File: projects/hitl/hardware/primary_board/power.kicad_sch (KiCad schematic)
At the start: 11 parts

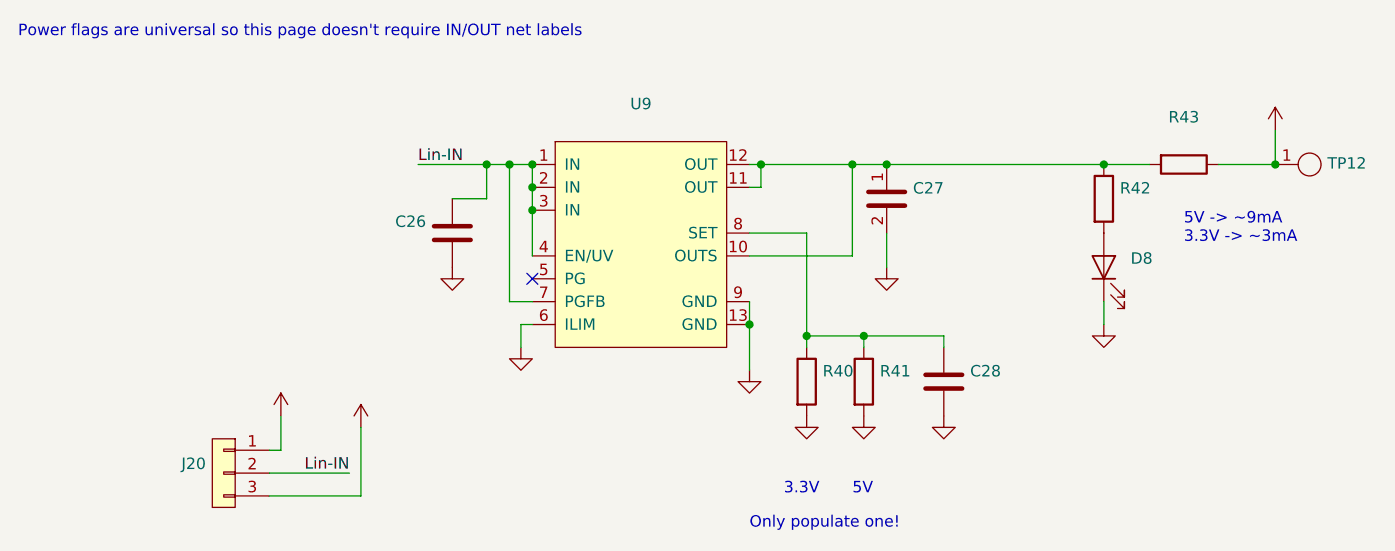
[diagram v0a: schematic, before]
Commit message: chore: annotate migrated schematics
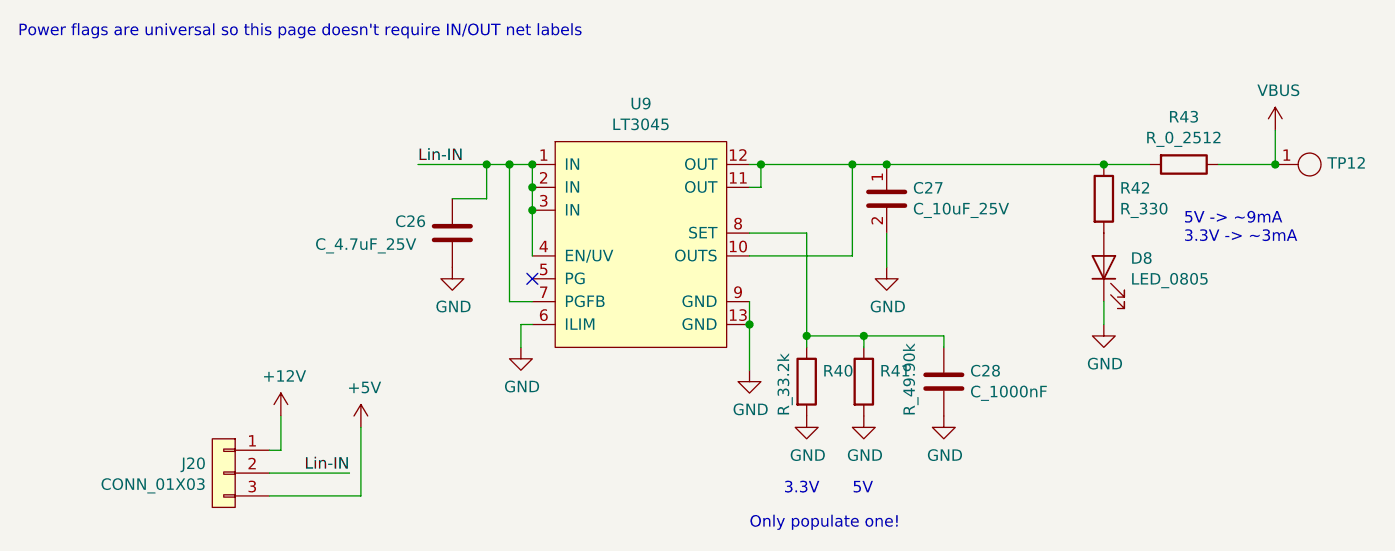
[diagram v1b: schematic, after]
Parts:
- C26: value (none) -> C_4.7uF_25V; footprint (none) -> footprints:C_0805_OEM
- C27: value (none) -> C_10uF_25V; footprint (none) -> footprints:C_0805_OEM
- C28: value (none) -> C_1000nF; footprint (none) -> footprints:C_0603_1608Metric
- D8: value (none) -> LED_0805; footprint (none) -> footprints:LED_0805_OEM
- J20: value (none) -> CONN_01X03; footprint (none) -> footprints:PinHeader_1x03_P2.54mm_Vertical
- R40: value (none) -> R_33.2k; footprint (none) -> footprints:R_0805_OEM
- R41: value (none) -> R_49.90k; footprint (none) -> footprints:R_0805_OEM
- R42: value (none) -> R_330; footprint (none) -> footprints:R_0805_OEM
- R43: value (none) -> R_0_2512; footprint (none) -> footprints:R_2512_OEM
- TP12: value (none) -> Test_Point_SMD; footprint (none) -> footprints:Test_Point_SMD
- U9: value (none) -> LT3045; footprint (none) -> footprints:MSOP-12_MSE
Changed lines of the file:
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@@
     (in_bom yes) (on_board yes)
     (property "Reference" "U9" (id 0) (at 140.335 59.309 0))
-    (property "Value" "" (id 1) (at 140.335 61.6204 0))
-    (property "Footprint" "" (id 2) (at 121.92 17.78 0)
+    (property "Value" "LT3045" (id 1) (at 140.335 61.6204 0))
+    (property "Footprint" "footprints:MSOP-12_MSE" (id 2) (at 121.92 17.78 0)
       (effects (font (size 1.27 1.27) italic) hide)
     )
@@
       (effects (font (size 1.27 1.27)) hide)
     )
-    (property "Value" "" (id 1) (at 109.601 90.8558 0))
+    (property "Value" "+5V" (id 1) (at 109.601 90.8558 0))
     (property "Footprint" "" (id 2) (at 109.22 95.25 0)
       (effects (font (size 1.27 1.27)) hide)
@@
       (effects (font (size 1.27 1.27)) hide)
     )
-    (property "Value" "" (id 1) (at 211.201 57.8358 0))
+    (property "Value" "VBUS" (id 1) (at 211.201 57.8358 0))
     (property "Footprint" "" (id 2) (at 210.82 62.23 0)
       (effects (font (size 1.27 1.27)) hide)
@@
       (effects (font (size 1.27 1.27)) (justify left))
     )
-    (property "Value" "" (id 1) (at 104.14 74.93 0)
-      (effects (font (size 1.27 1.27)) (justify left))
-    )
-    (property "Footprint" "" (id 2) (at 120.3452 59.69 0)
+    (property "Value" "C_4.7uF_25V" (id 1) (at 104.14 74.93 0)
+      (effects (font (size 1.27 1.27)) (justify left))
+    )
+    (property "Footprint" "footprints:C_0805_OEM" (id 2) (at 120.3452 59.69 0)
       (effects (font (size 1.27 1.27)) hide)
     )
@@
       (effects (font (size 1.27 1.27)) hide)
     )
-    (property "Value" "" (id 1) (at 119.507 81.8642 0))
+    (property "Value" "GND" (id 1) (at 119.507 81.8642 0))
     (property "Footprint" "" (id 2) (at 119.38 77.47 0)
       (effects (font (size 1.27 1.27)) hide)
@@
       (effects (font (size 1.27 1.27)) hide)
     )
-    (property "Value" "" (id 1) (at 127.127 90.7542 0))
+    (property "Value" "GND" (id 1) (at 127.127 90.7542 0))
     (property "Footprint" "" (id 2) (at 127 86.36 0)
       (effects (font (size 1.27 1.27)) hide)
@@
       (effects (font (size 1.27 1.27)) (justify left))
     )
-    (property "Value" "" (id 1) (at 170.561 70.993 0)
-      (effects (font (size 1.27 1.27)) (justify left))
-    )
-    (property "Footprint" "" (id 2) (at 166.37 74.93 0)
+    (property "Value" "C_10uF_25V" (id 1) (at 170.561 70.993 0)
+      (effects (font (size 1.27 1.27)) (justify left))
+    )
+    (property "Footprint" "footprints:C_0805_OEM" (id 2) (at 166.37 74.93 0)
       (effects (font (size 1.27 1.27)) hide)
     )
@@
       (effects (font (size 1.27 1.27)) hide)
     )
-    (property "Value" "" (id 1) (at 152.527 93.2942 0))
+    (property "Value" "GND" (id 1) (at 152.527 93.2942 0))
     (property "Footprint" "" (id 2) (at 152.4 88.9 0)
       (effects (font (size 1.27 1.27)) hide)
@@
       (effects (font (size 1.27 1.27)) hide)
     )
-    (property "Value" "" (id 1) (at 100.711 89.5858 0))
+    (property "Value" "+12V" (id 1) (at 100.711 89.5858 0))
     (property "Footprint" "" (id 2) (at 100.33 93.98 0)
       (effects (font (size 1.27 1.27)) hide)
@@
       (effects (font (size 1.27 1.27)) (justify left))
     )
-    (property "Value" "" (id 1) (at 91.9988 101.6 0)
-      (effects (font (size 1.27 1.27)) (justify left))
-    )
-    (property "Footprint" "" (id 2) (at 92.71 130.81 0)
+    (property "Value" "CONN_01X03" (id 1) (at 91.9988 101.6 0)
+      (effects (font (size 1.27 1.27)) (justify left))
+    )
+    (property "Footprint" "footprints:PinHeader_1x03_P2.54mm_Vertical" (id 2) (at 92.71 130.81 0)
       (effects (font (size 1.27 1.27)) hide)
     )
@@
       (effects (font (size 1.27 1.27)) (justify left))
     )
-    (property "Value" "" (id 1) (at 170.18 93.98 90)
-      (effects (font (size 1.27 1.27)) (justify left))
-    )
-    (property "Footprint" "" (id 2) (at 163.322 77.47 0)
+    (property "Value" "R_49.90k" (id 1) (at 170.18 93.98 90)
+      (effects (font (size 1.27 1.27)) (justify left))
+    )
+    (property "Footprint" "footprints:R_0805_OEM" (id 2) (at 163.322 77.47 0)
       (effects (font (size 1.27 1.27)) hide)
     )
@@
       (effects (font (size 1.27 1.27)) (justify left))
     )
-    (property "Value" "" (id 1) (at 156.21 93.98 90)
-      (effects (font (size 1.27 1.27)) (justify left))
-    )
-    (property "Footprint" "" (id 2) (at 156.972 77.47 0)
+    (property "Value" "R_33.2k" (id 1) (at 156.21 93.98 90)
+      (effects (font (size 1.27 1.27)) (justify left))
+    )
+    (property "Footprint" "footprints:R_0805_OEM" (id 2) (at 156.972 77.47 0)
       (effects (font (size 1.27 1.27)) hide)
     )
@@
       (effects (font (size 1.27 1.27)) hide)
     )
-    (property "Value" "" (id 1) (at 165.227 98.3742 0))
+    (property "Value" "GND" (id 1) (at 165.227 98.3742 0))
     (property "Footprint" "" (id 2) (at 165.1 93.98 0)
       (effects (font (size 1.27 1.27)) hide)
@@
       (effects (font (size 1.27 1.27)) hide)
     )
-    (property "Value" "" (id 1) (at 158.877 98.3742 0))
+    (property "Value" "GND" (id 1) (at 158.877 98.3742 0))
     (property "Footprint" "" (id 2) (at 158.75 93.98 0)
       (effects (font (size 1.27 1.27)) hide)
@@
       (effects (font (size 1.27 1.27)) (justify left))
     )
-    (property "Value" "" (id 1) (at 176.911 91.313 0)
-      (effects (font (size 1.27 1.27)) (justify left))
-    )
-    (property "Footprint" "" (id 2) (at 174.9552 93.98 0)
+    (property "Value" "C_1000nF" (id 1) (at 176.911 91.313 0)
+      (effects (font (size 1.27 1.27)) (justify left))
+    )
+    (property "Footprint" "footprints:C_0603_1608Metric" (id 2) (at 174.9552 93.98 0)
       (effects (font (size 1.27 1.27)) hide)
     )
@@
       (effects (font (size 1.27 1.27)) hide)
     )
-    (property "Value" "" (id 1) (at 167.767 81.8642 0))
+    (property "Value" "GND" (id 1) (at 167.767 81.8642 0))
     (property "Footprint" "" (id 2) (at 167.64 77.47 0)
       (effects (font (size 1.27 1.27)) hide)
@@
       (effects (font (size 1.27 1.27)) hide)
     )
-    (property "Value" "" (id 1) (at 174.117 98.3742 0))
+    (property "Value" "GND" (id 1) (at 174.117 98.3742 0))
     (property "Footprint" "" (id 2) (at 173.99 93.98 0)
       (effects (font (size 1.27 1.27)) hide)
@@
     (in_bom yes) (on_board yes)
     (property "Reference" "R43" (id 0) (at 200.66 60.7822 90))
-    (property "Value" "" (id 1) (at 200.66 63.0936 90))
-    (property "Footprint" "" (id 2) (at 200.66 64.262 0)
+    (property "Value" "R_0_2512" (id 1) (at 200.66 63.0936 90))
+    (property "Footprint" "footprints:R_2512_OEM" (id 2) (at 200.66 64.262 0)
       (effects (font (size 1.27 1.27)) hide)
     )
@@
       (effects (font (size 1.27 1.27)) (justify right))
     )
-    (property "Value" "" (id 1) (at 194.7418 78.7908 90)
+    (property "Value" "LED_0805" (id 1) (at 194.7418 78.7908 90)
       (effects (font (size 1.27 1.27)) (justify right))
     )
-    (property "Footprint" "" (id 2) (at 191.77 80.01 0)
+    (property "Footprint" "footprints:LED_0805_OEM" (id 2) (at 191.77 80.01 0)
       (effects (font (size 1.27 1.27)) hide)
     )
@@
       (effects (font (size 1.27 1.27)) (justify left))
     )
-    (property "Value" "" (id 1) (at 193.548 70.993 0)
-      (effects (font (size 1.27 1.27)) (justify left))
-    )
-    (property "Footprint" "" (id 2) (at 189.992 69.85 0)
+    (property "Value" "R_330" (id 1) (at 193.548 70.993 0)
+      (effects (font (size 1.27 1.27)) (justify left))
+    )
+    (property "Footprint" "footprints:R_0805_OEM" (id 2) (at 189.992 69.85 0)
       (effects (font (size 1.27 1.27)) hide)
     )
@@
       (effects (font (size 1.27 1.27)) hide)
     )
-    (property "Value" "" (id 1) (at 191.897 88.2142 0))
+    (property "Value" "GND" (id 1) (at 191.897 88.2142 0))
     (property "Footprint" "" (id 2) (at 191.77 83.82 0)
       (effects (font (size 1.27 1.27)) hide)
@@
       (effects (font (size 1.27 1.27)) (justify left))
     )
-    (property "Value" "" (id 1) (at 212.0138 68.0212 0)
+    (property "Value" "Test_Point_SMD" (id 1) (at 212.0138 68.0212 0)
       (effects (font (size 1.27 1.27)) (justify left) hide)
     )
-    (property "Footprint" "" (id 2) (at 208.28 66.04 0)
-      (effects (font (size 1.27 1.27)) hide)
-    )
+    (property "Footprint" "footprints:Test_Point_SMD" (id 2) (at 208.28 66.04 0)
+      (effects (font (size 1.27 1.27)) hide)
+    )

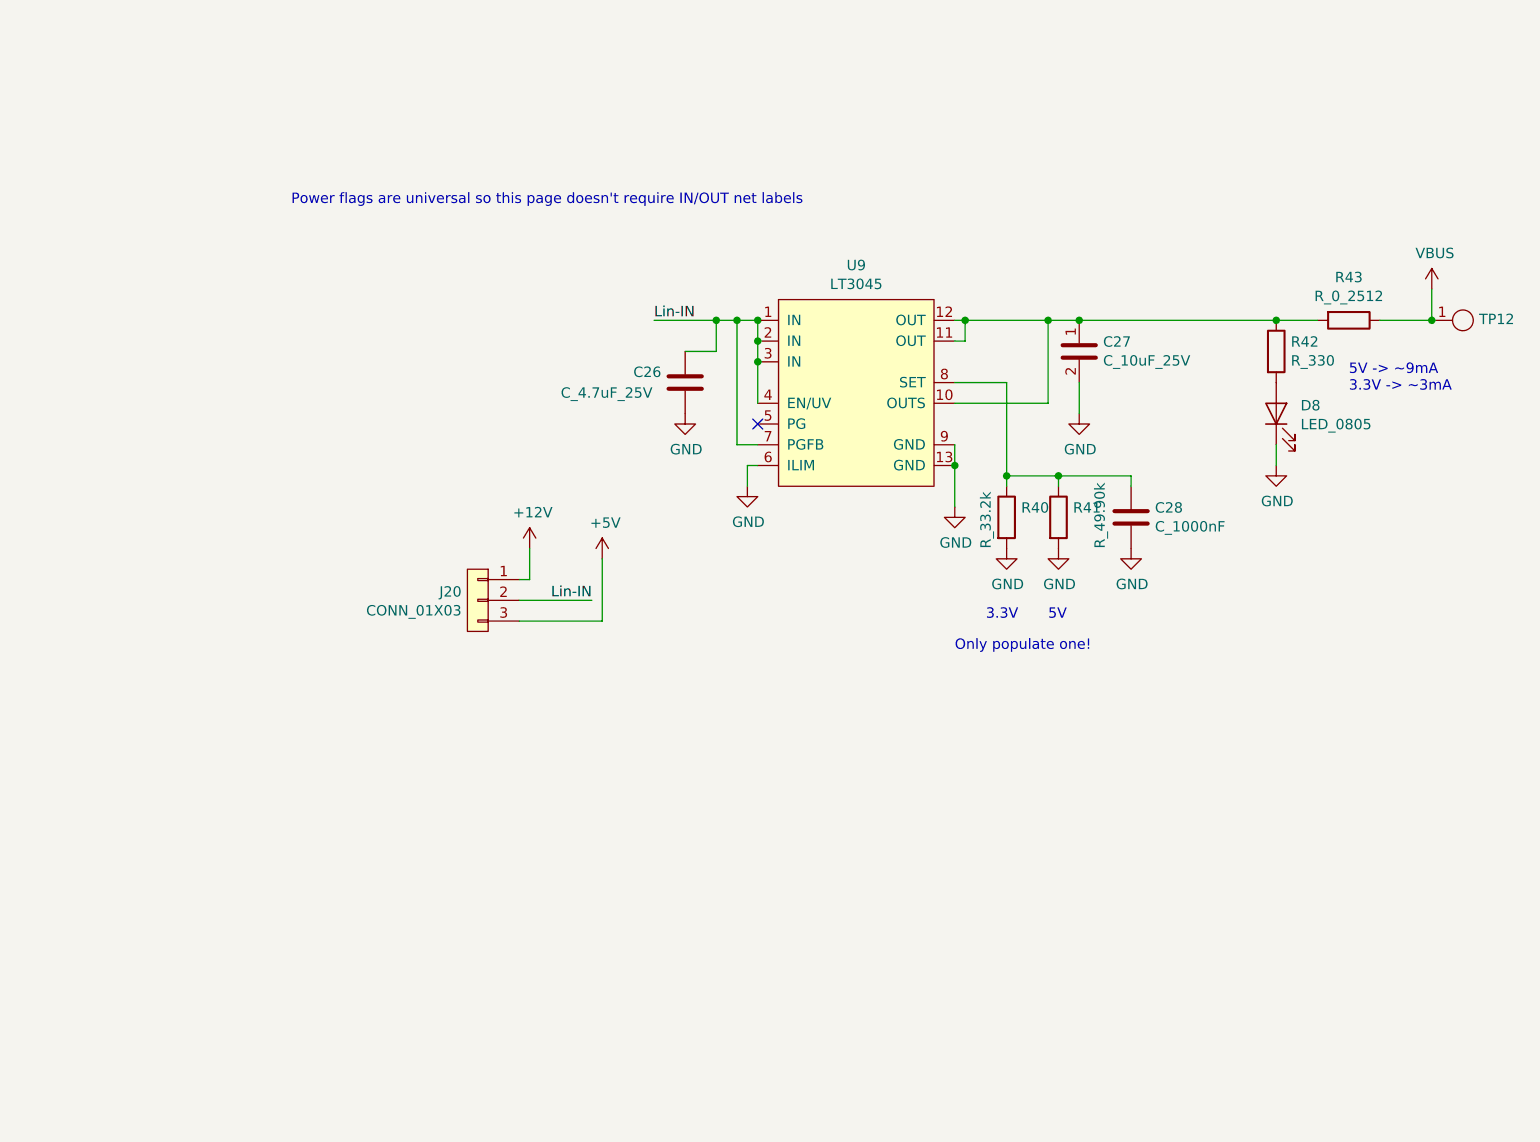
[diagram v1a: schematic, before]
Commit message: Hardware-in-the-loop primary rev 1.1 (#172)
* Split schematic into sheets

* Switch FTPROG to button and update I2C level shifter

* Fix footprint for FTDI chip

* Replace zero-ohm resistors with solder jumpers

* Changes from feedback
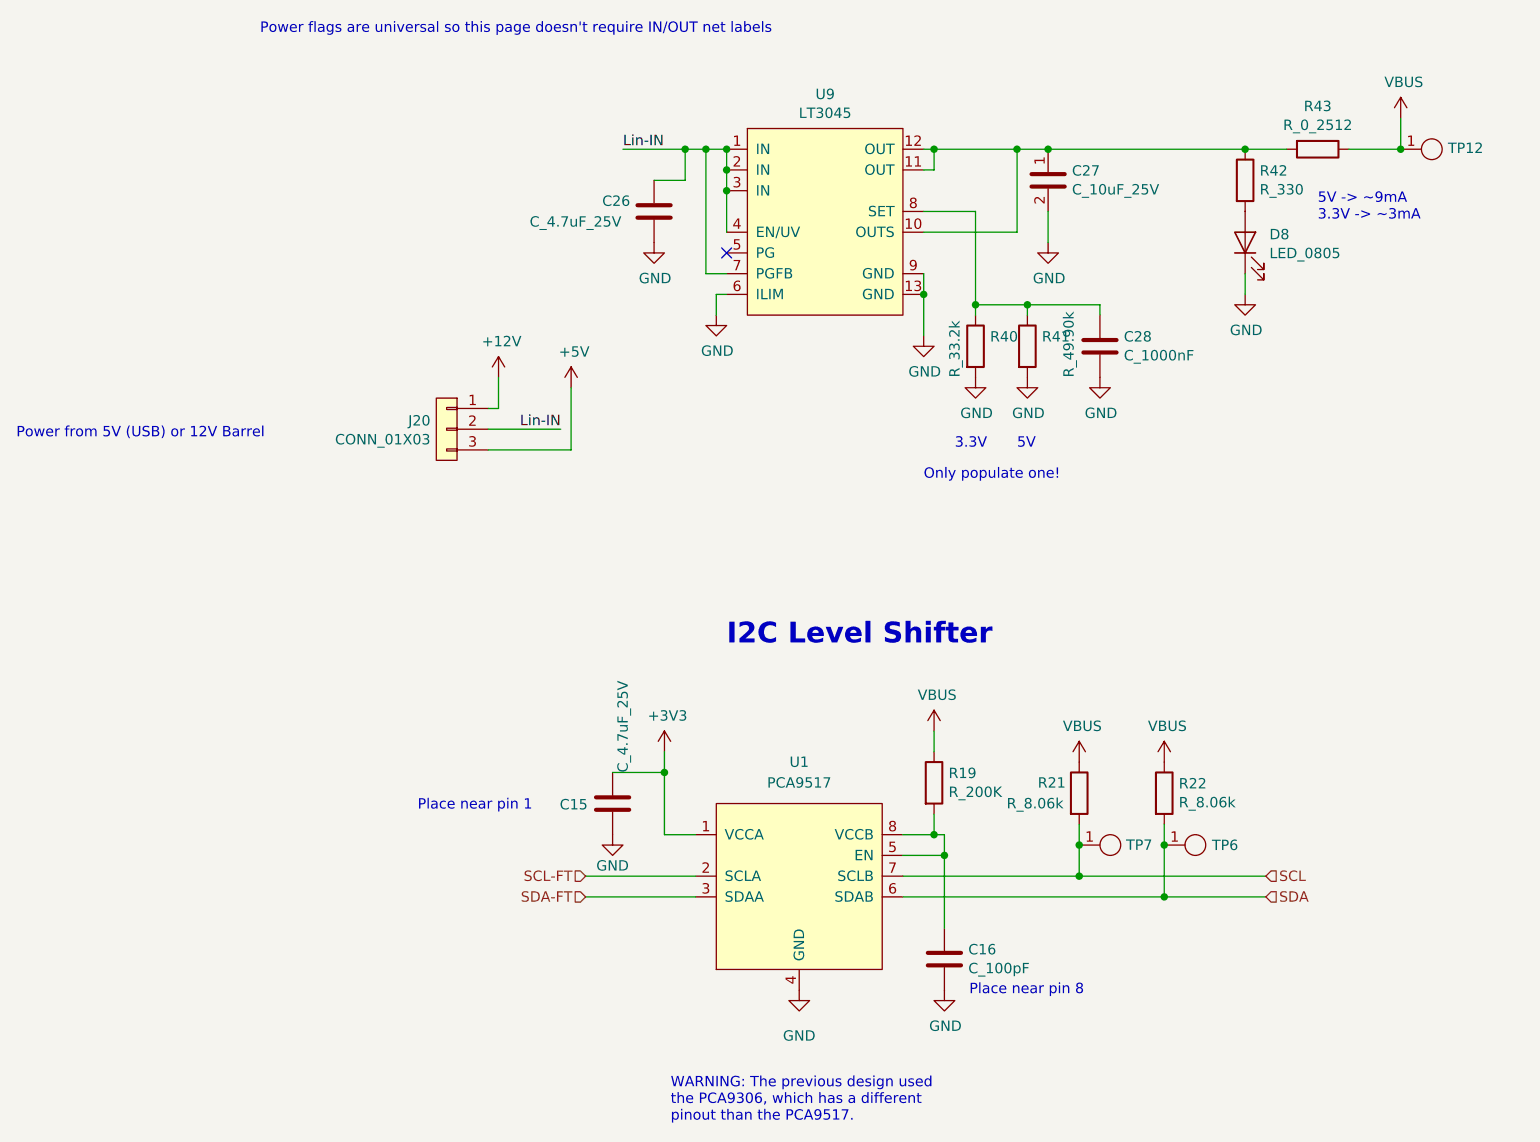
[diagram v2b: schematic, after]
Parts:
- added C15: C_4.7uF_25V, footprints:C_0805_OEM, symbol formula:C_4.7uF_25V
- added C16: C_100pF, footprints:C_0805_OEM, symbol formula:C_100pF
- added R19: R_200K, footprints:R_0805_OEM, symbol formula:R_200K
- added R21, R22: R_8.06k, footprints:R_0805_OEM, symbol formula:R_8.06k
- added TP6, TP7: Test_Point_SMD, footprints:Test_Point_SMD, symbol formula:Test_Point_SMD
- added U1: PCA9517, footprints:Micro8_PCA9517, symbol formula:PCA9517
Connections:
- net GND: now also C15.2, C16.2, U1.4 (GND)
- net VBUS: now also R19.1, R21.1, R22.1
- new net: C16.1, R19.2, U1.5 (EN), U1.8 (VCCB)
- new net +3V3: C15.1, U1.1 (VCCA)
- new net SCL: R21.2, TP7.1, U1.7 (SCLB)
- new net SCL-FT: U1.2 (SCLA)
- new net SDA: R22.2, TP6.1, U1.6 (SDAB)
- new net SDA-FT: U1.3 (SDAA)
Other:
- note added: "I2C Level Shifter"
- note added: "Place near pin 1"
- note added: "Place near pin 8"
- note added: "Power from 5V (USB) or 12V Barrel"
- note added: "WARNING: The previous design used the PCA9306, which has a different pinout than the PCA9517."
- moved on the sheet: C26, C27, C28, D8, J20, R40, R41, R42, R43, TP12, U9
